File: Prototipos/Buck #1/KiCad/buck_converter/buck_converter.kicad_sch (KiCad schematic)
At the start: 32 parts, among them J1 Screw_Terminal_01x02, J2 Conn_01x03_Pin, J3 Screw_Terminal_01x02, Q1 NPN, Q2 IRF9540NPBF, Q3 IRLML6344

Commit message: Primeros avances con PCB de Buck
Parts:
- C7: renamed from C8; value (none) -> ~
- D1: footprint Diode_THT:D_A-405_P10.16mm_Horizontal -> Diode_THT:D_DO-34_SOD68_P7.62mm_Horizontal
- D2: renamed from D3; footprint Diode_THT:D_A-405_P10.16mm_Horizontal -> Diode_THT:D_DO-34_SOD68_P7.62mm_Horizontal
- D3: renamed from D4; footprint Diode_THT:D_A-405_P10.16mm_Horizontal -> Diode_THT:D_DO-34_SOD68_P7.62mm_Horizontal
- D4: renamed from D5; footprint Diode_THT:D_A-405_P10.16mm_Horizontal -> Diode_THT:D_DO-34_SOD68_P7.62mm_Horizontal
- J1: renamed from J2; footprint (none) -> Connector_PinHeader_2.54mm:PinHeader_1x03_P2.54mm_Vertical
- J2: renamed from J1; footprint TerminalBlock_Phoenix:TerminalBlock_Phoenix_MPT-0,5-2-2.54_1x02_P2.54mm_Horizontal -> TerminalBlock_TE-Connectivity:TerminalBlock_TE_282834-2_1x02_P2.54mm_Horizontal
- J3: footprint TerminalBlock_Phoenix:TerminalBlock_Phoenix_MPT-0,5-2-2.54_1x02_P2.54mm_Horizontal -> TerminalBlock_TE-Connectivity:TerminalBlock_TE_282834-2_1x02_P2.54mm_Horizontal
- Q1: renamed from Q2; footprint KICAD-Libraries:TO254P1052X465X1989-3 -> KICAD-Libraries:TO254P470X1000X2000-3P
- Q2: renamed from Q3; footprint IRLML6344:SOT23 -> KICAD-Libraries:SOT23
- Q3: renamed from Q1; footprint (none) -> Package_TO_SOT_THT:TO-92_Inline
- R1: renamed from R11; footprint Resistor_THT:R_Axial_DIN0207_L6.3mm_D2.5mm_P15.24mm_Horizontal -> Resistor_THT:R_Axial_DIN0207_L6.3mm_D2.5mm_P7.62mm_Horizontal
- R10, R7, R8, R9: footprint Resistor_THT:R_Axial_DIN0207_L6.3mm_D2.5mm_P15.24mm_Horizontal -> Resistor_THT:R_Axial_DIN0207_L6.3mm_D2.5mm_P7.62mm_Horizontal
- R11: renamed from R15; value (none) -> ~; footprint Resistor_THT:R_Axial_DIN0207_L6.3mm_D2.5mm_P15.24mm_Horizontal -> Resistor_THT:R_Axial_DIN0207_L6.3mm_D2.5mm_P7.62mm_Horizontal
- R12: renamed from R16; value (none) -> ~; footprint Resistor_THT:R_Axial_DIN0207_L6.3mm_D2.5mm_P15.24mm_Horizontal -> Resistor_THT:R_Axial_DIN0207_L6.3mm_D2.5mm_P7.62mm_Horizontal
- R13: renamed from R17; footprint Resistor_THT:R_Axial_DIN0207_L6.3mm_D2.5mm_P15.24mm_Horizontal -> Resistor_THT:R_Axial_DIN0207_L6.3mm_D2.5mm_P7.62mm_Horizontal
- R14: renamed from R18; value (none) -> ~; footprint Resistor_THT:R_Axial_DIN0207_L6.3mm_D2.5mm_P15.24mm_Horizontal -> Resistor_THT:R_Axial_DIN0207_L6.3mm_D2.5mm_P7.62mm_Horizontal
- R2: renamed from R4; footprint Resistor_THT:R_Axial_DIN0207_L6.3mm_D2.5mm_P15.24mm_Horizontal -> Resistor_THT:R_Axial_DIN0207_L6.3mm_D2.5mm_P7.62mm_Horizontal
- R3: renamed from R12; footprint Resistor_THT:R_Axial_DIN0207_L6.3mm_D2.5mm_P15.24mm_Horizontal -> Resistor_THT:R_Axial_DIN0207_L6.3mm_D2.5mm_P7.62mm_Horizontal
- R4: renamed from R13; footprint Resistor_THT:R_Axial_DIN0207_L6.3mm_D2.5mm_P15.24mm_Horizontal -> Resistor_THT:R_Axial_DIN0207_L6.3mm_D2.5mm_P7.62mm_Horizontal
- R5: renamed from R6; footprint Resistor_THT:R_Axial_DIN0207_L6.3mm_D2.5mm_P15.24mm_Horizontal -> Resistor_THT:R_Axial_DIN0207_L6.3mm_D2.5mm_P7.62mm_Horizontal
- R6: renamed from R14; footprint Resistor_THT:R_Axial_DIN0207_L6.3mm_D2.5mm_P15.24mm_Horizontal -> Resistor_THT:R_Axial_DIN0207_L6.3mm_D2.5mm_P7.62mm_Horizontal
- renumbered C4 to C3, C7 to C4

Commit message: Avances en PCB convertidor buck
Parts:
- added J4, J5, J6: Conn_01x03_Pin, Connector_PinHeader_2.54mm:PinHeader_1x03_P2.54mm_Vertical, symbol Connector:Conn_01x03_Pin
- J2, J3: footprint TerminalBlock_TE-Connectivity:TerminalBlock_TE_282834-2_1x02_P2.54mm_Horizontal -> TerminalBlock_Phoenix:TerminalBlock_Phoenix_MKDS-1,5-2-5.08_1x02_P5.08mm_Horizontal
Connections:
- net 12V: now also D1.1 (K), J2.1 (Pin_1), Q1.3, R2.1, J6.2 (Pin_2); no longer R12.1, R3.1
- net Gate: now also J5.2 (Pin_2); no longer D3.1 (K), D4.1 (K), Q2.3, Q3.1 (C), R12.2, R14.1, R3.2, R6.1
- net PWM_micro: now also J4.2 (Pin_2); no longer R1.1, R11.1
- new net 12V_BJT: J6.1 (Pin_1), R12.1
- new net 12V_MOSFET: J6.3 (Pin_3), R3.1
- new net Gate_BJT: D4.1 (K), J5.1 (Pin_1), Q3.1 (C), R12.2, R14.1
- new net Gate_MOSFET: D3.1 (K), J5.3 (Pin_3), Q2.3, R3.2, R6.1
- new net PWM_BJT: J4.1 (Pin_1), R11.1
- new net PWM_MOSFET: J4.3 (Pin_3), R1.1
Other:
- moved on the sheet: C1, C4, C7, D3, D4, Q2, Q3, R1, R11, R12, R13, R14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

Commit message: Actualización de PCB
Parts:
- C7: value ~ -> 2p
- R11: value ~ -> 33k
- R12: value ~ -> 120
- R14: value ~ -> 180
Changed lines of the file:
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@@
 			)
 		)
-		(property "Value" "~"
+		(property "Value" "33k"
 			(at 162.56 119.888 90)
 			(effects
@@
 			)
 		)
-		(property "Value" "~"
+		(property "Value" "180"
 			(at 189.992 113.03 90)
 			(effects
@@
 			)
 		)
-		(property "Value" "~"
+		(property "Value" "2p"
 			(at 194.818 123.19 90)
 			(effects
@@
 			)
 		)
-		(property "Value" "~"
+		(property "Value" "120"
 			(at 167.132 107.95 0)
 			(effects

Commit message: Corrección footprint transistor
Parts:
- Q3: footprint Package_TO_SOT_THT:TO-92_Inline -> Package_TO_SOT_THT:TO-92_Inline_Wide
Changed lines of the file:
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@@
 			)
 		)
-		(property "Footprint" "Package_TO_SOT_THT:TO-92_Inline"
+		(property "Footprint" "Package_TO_SOT_THT:TO-92_Inline_Wide"
 			(at 237.49 118.11 0)
 			(effects

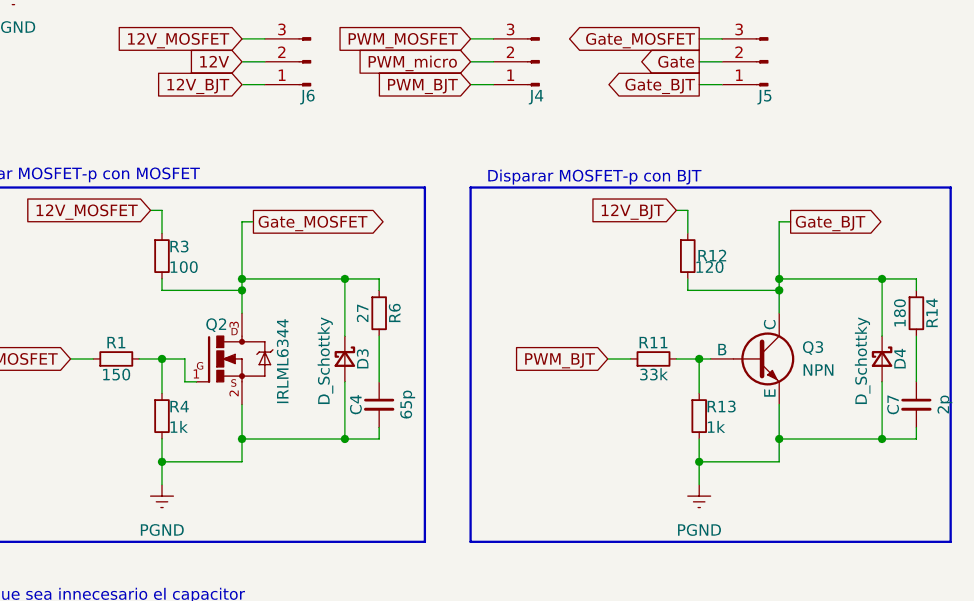
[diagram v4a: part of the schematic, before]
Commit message: Corrección PCB Buck, para disminuir tamaño
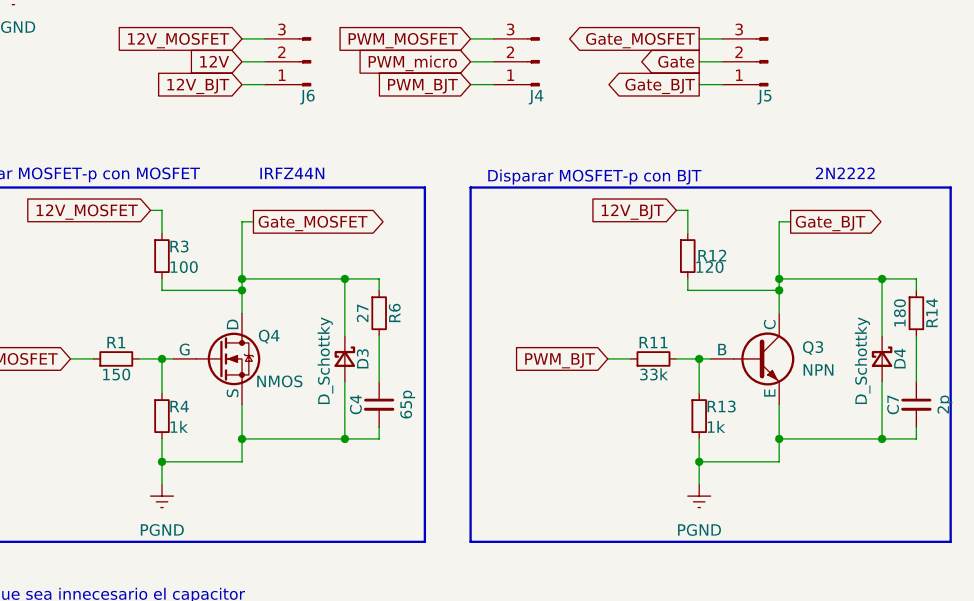
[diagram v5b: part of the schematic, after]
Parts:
- removed Q2: IRLML6344, KICAD-Libraries:SOT23, symbol IRLML6344:IRLML6344
- added Q4: NMOS, Package_TO_SOT_THT:TO-220-3_Vertical, symbol Simulation_SPICE:NMOS
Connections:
- net Gate_BJT: now also Q3.3 (C); no longer Q3.1 (C)
- net Gate_MOSFET: now also Q4.2 (D)
- net PGND: now also Q3.1 (E), Q4.3 (S); no longer Q3.3 (E)
- net at R1.2, R4.1: now also Q4.1 (G)
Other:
- note added: "2N2222"
- note added: "IRFZ44N"
